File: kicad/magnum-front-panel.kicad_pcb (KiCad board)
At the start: 2 copper layers, 101.3 x 128.5 mm, 4 parts

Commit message: Update front panel with new design
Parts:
- added Ref**: Val**, magnum-panel:magnum-panel-layers, F.Cu at (31.0, 20.0)
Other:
- board size 101.3 x 128.5 mm -> 101.3 x 128.6 mm

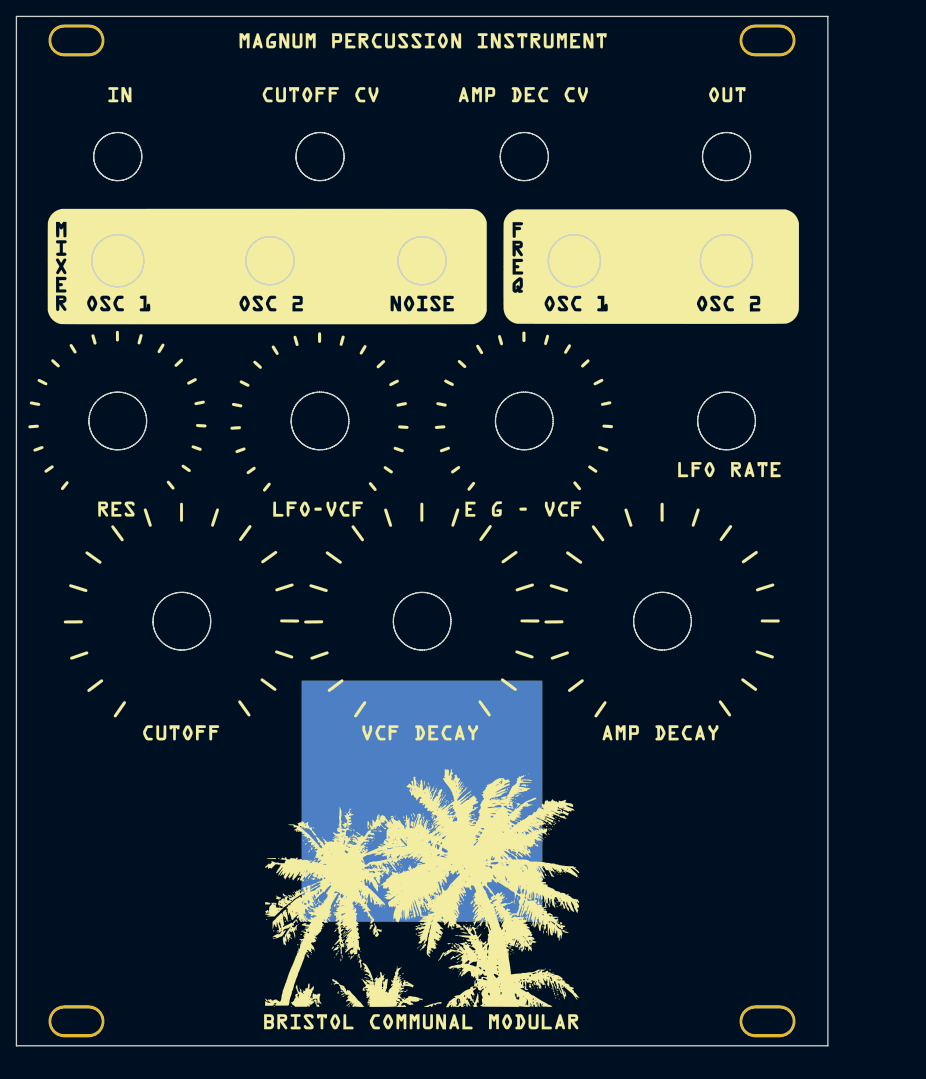
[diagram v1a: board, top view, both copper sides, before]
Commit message: Adding files for next revision of front panel
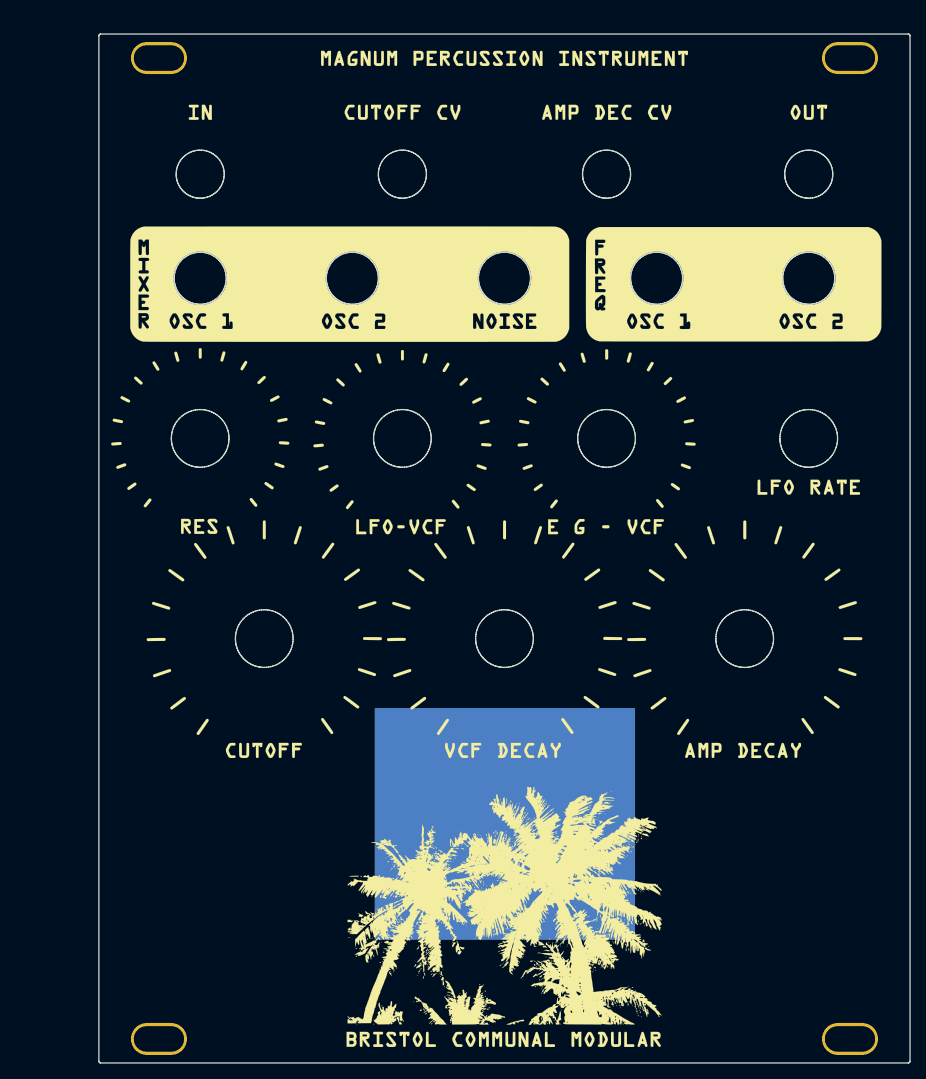
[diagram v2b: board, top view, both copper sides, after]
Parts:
- removed REF** (x4): PanelHole_3.2mm_M3_elongated, Rumblesan_Footprints:PanelHole_3.2mm_M3_elongated
- removed the Ref** at (31.0, 20.0)
- added Ref**: Val**, magnum-panel:magnum-palmtree-panel, F.Cu at (41.3, 22.2)
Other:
- board size 101.3 x 128.6 mm -> 101.3 x 128.5 mm
